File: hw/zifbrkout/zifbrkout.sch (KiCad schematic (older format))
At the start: 122 parts, among them J1 501951-4000

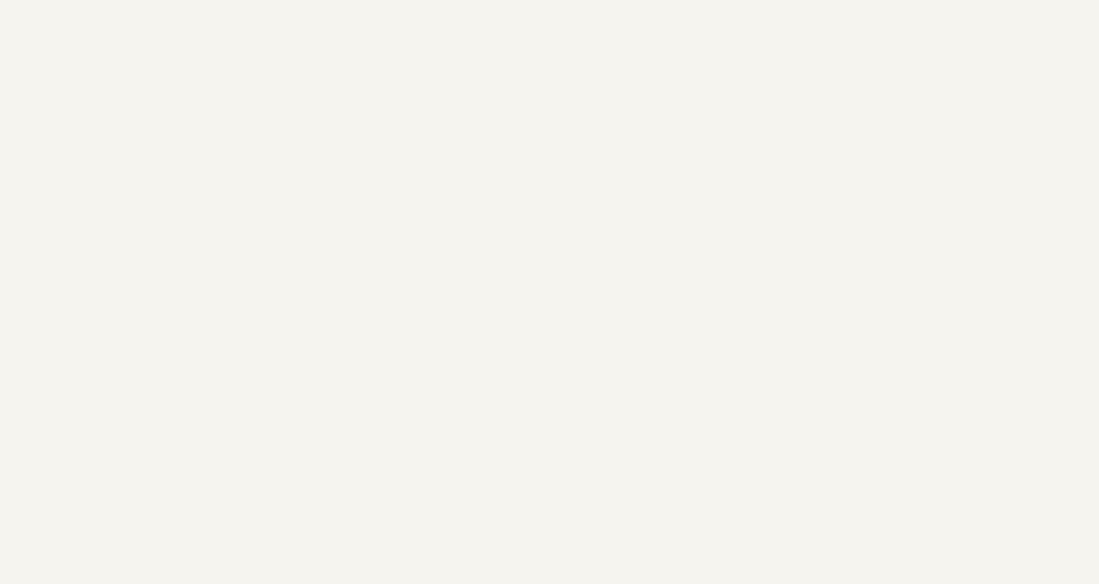
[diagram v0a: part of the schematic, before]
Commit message: added copyright notices added COPYING file with GPL v2 license added README file moved font files
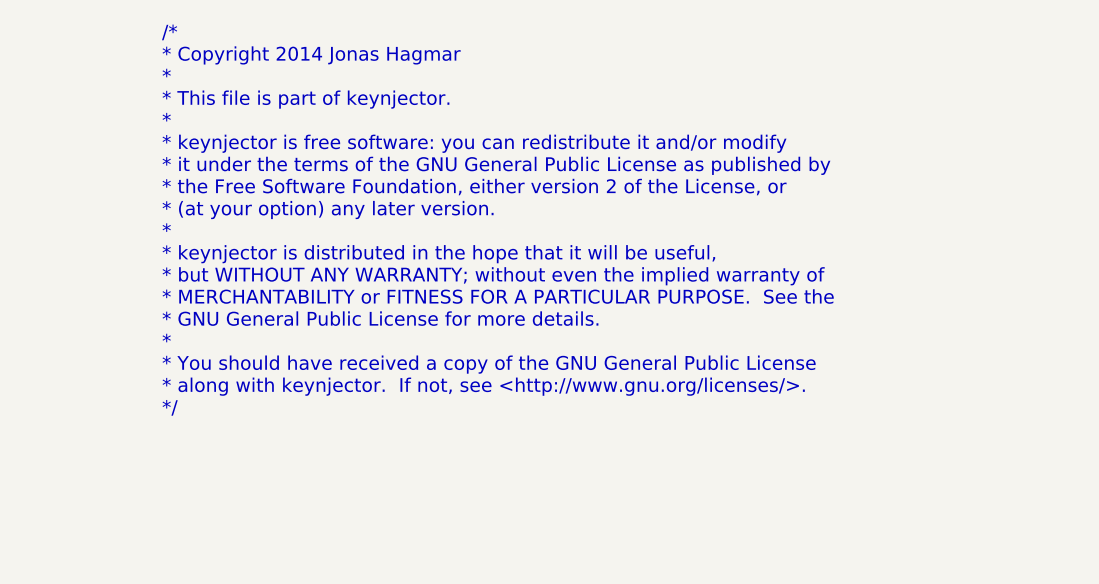
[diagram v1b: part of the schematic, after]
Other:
- note added: "/*\n* Copyright 2014 Jonas Hagmar\n*\n* This file is part of keynjector.\n*\n* keynjector is free software: you can redistribute it and/or modify\n* it under the terms of the GNU General Public License as published by\n* the Free Software Foundation, either version 2 of the License, or\n* (at your option) any later version.\n*\n* keynjector is distributed in the hope that it will be useful,\n* bu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"
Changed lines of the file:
@@
 Sheet 1 1
 Title ""
-Date "3 aug 2014"
+Date "5 dec 2014"
 Rev ""
 Comp ""
@@
 	1    0    0    -1
 $EndComp
+Text Notes 4900 2250 0    60   ~ 0
+/*\n* Copyright 2014 Jonas Hagmar\n*\n* This file is part of keynjector.\n*\n* keynjector is free software: you can redistribute it and/or modify\n* it under the terms of the GNU General Public License as published by\n* the Free Software Foundation, either version 2 of the License, or\n* (at your option) any later version.\n*\n* keynjector is distributed in the hope that it will be useful,\n* but WITHOUT ANY WARRANTY; without even the implied warranty of\n* MERCHANTABILITY or FITNESS FOR A PARTICULAR PURPOSE.  See the\n* GNU General Public License for more details.\n*\n* You should have received a copy of the GNU General Public License\n* along with keynjector.  If not, see <http://www.gnu.org/licenses/>.\n*/
 $EndSCHEMATC
